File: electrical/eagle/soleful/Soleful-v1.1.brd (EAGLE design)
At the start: 50.5 x 59.7 mm, 118 parts, among them CN1 To Battery, CN2 Ext Power, IC1 STM32F405RGT, IC2 LT1129-3.3, IC3 MCP73833-UN, Q4 32.768kHz, SW1 RST, U1 USB Power, U2 TPD3E001DRLR, Y1 12 MHz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

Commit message: finished board layout bitch
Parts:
- moved U2 129.9 mm to (10.8, 5.71)
- moved R30 124.3 mm to (35.2, 17.4), turned to 180 degrees
- moved R14 123.1 mm to (45.1, 22.9), turned to 180 degrees
- moved R23 120.3 mm to (35.2, 18.6), turned to 180 degrees
- moved R12 113.7 mm to (44.5, 27.9)
- moved R11 110.8 mm to (44.5, 25.4)
- moved R15 104.1 mm to (18.7, 16.8), turned to 90 degrees
- moved TP6 97.0 mm to (41.2, 19.5)
- moved R10 96.1 mm to (17.3, 3.27), turned to 180 degrees
- moved TP4 93.9 mm to (48.9, 28.6)
- moved C10 93.6 mm to (36.1, 7.94), turned to 270 degrees
- moved R13 91.8 mm to (17.4, 27.3), turned to 180 degrees
- moved R3 91.8 mm to (37.5, 30.5)
- moved D6 90.9 mm to (10.2, 16.5), turned to 270 degrees
- moved TP3 90.7 mm to (48.9, 30.5)
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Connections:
- removed net N$19: U$18.10
- removed net N$23: R41.2
- net N$16: now also R41.2, U$18.10; no longer U$18.11
- net VDD-MMA: now also U$18.11
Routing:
- net 3V3: track 0.00 -> 267.1 mm, vias 0 -> 10
- net RST-WIFI: track 0.00 -> 145.7 mm, vias 0 -> 6
- net EN-WIFI: track 0.00 -> 144.1 mm, vias 0 -> 2
- net RX-WIFI: track 0.00 -> 97.2 mm, vias 0 -> 4
- net TX-WIFI: track 0.00 -> 94.9 mm, vias 0 -> 4
- net VDD-MMA: track 0.00 -> 62.6 mm, vias 0 -> 2
- net VUSB: track 0.00 -> 57.9 mm, vias 0 -> 4
- net RST-IMU: track 0.00 -> 57.3 mm, vias 0 -> 2
- net V+: track 0.00 -> 52.7 mm, vias 0 -> 2
- net PWR-IMU: track 0.00 -> 50.2 mm, vias 0 -> 6
- net PB2-BOOT1-MMA-INT: track 0.00 -> 48.0 mm, vias 0 -> 4
- net SCL-IMU: track 0.00 -> 43.5 mm, vias 0 -> 3
- net VCC-WIFI: track 0.00 -> 43.5 mm, vias 0 -> 2
- net PC11-SDIO_D3: track 0.00 -> 43.2 mm, vias 0 -> 2
- net SDA-IMU: track 0.00 -> 42.9 mm, vias 0 -> 2
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
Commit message: fixed all DRC issues
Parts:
- moved R30 0.27 mm to (35.2, 17.1)
- moved X1 0.13 mm to (9.02, 46.4)
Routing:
- net VCC-WIFI: track 43.5 -> 48.1 mm
- net 3V3: track 267.1 -> 265.2 mm, vias 10 -> 9
- net PWR-WIFI: track 42.3 -> 43.4 mm
- net PB2-BOOT1-MMA-INT: track 48.0 -> 48.7 mm
- net RST-WIFI: track 145.7 -> 146.3 mm

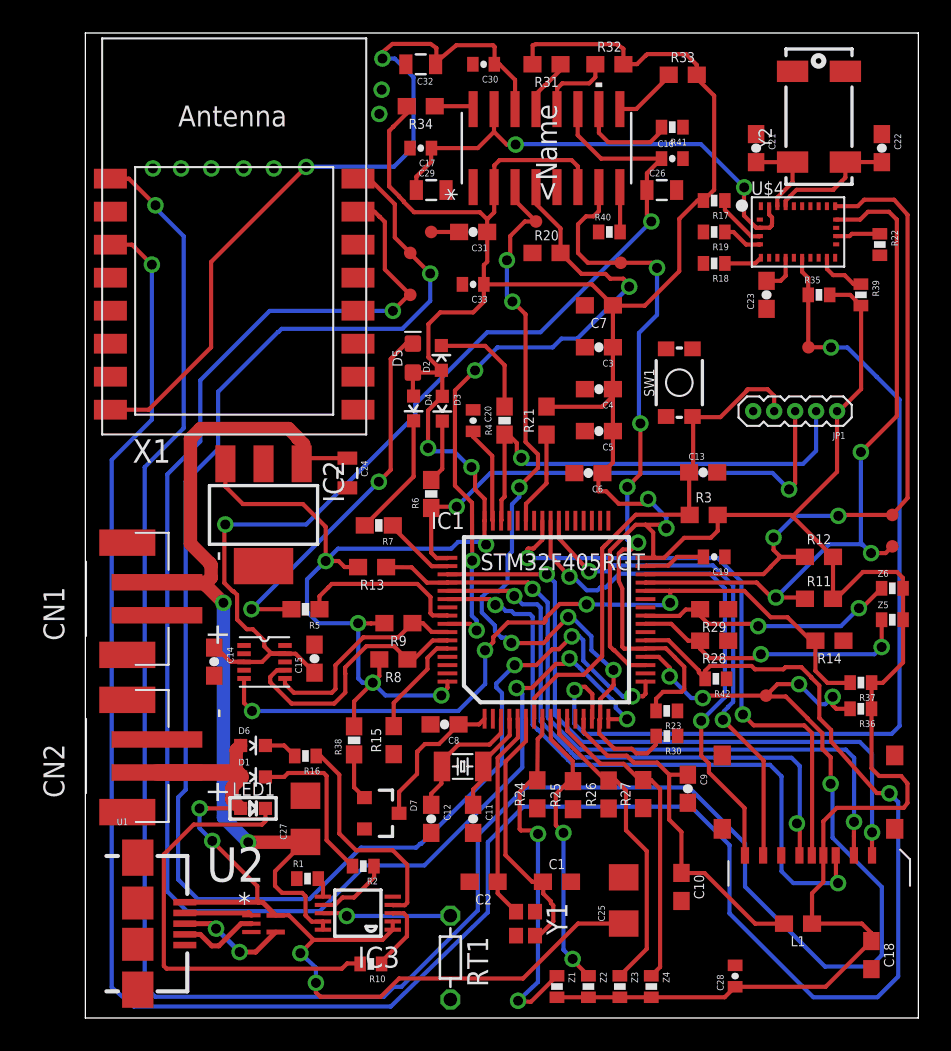
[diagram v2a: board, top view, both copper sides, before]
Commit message: finished the entire layout based on Sunstones DRC rules bitches
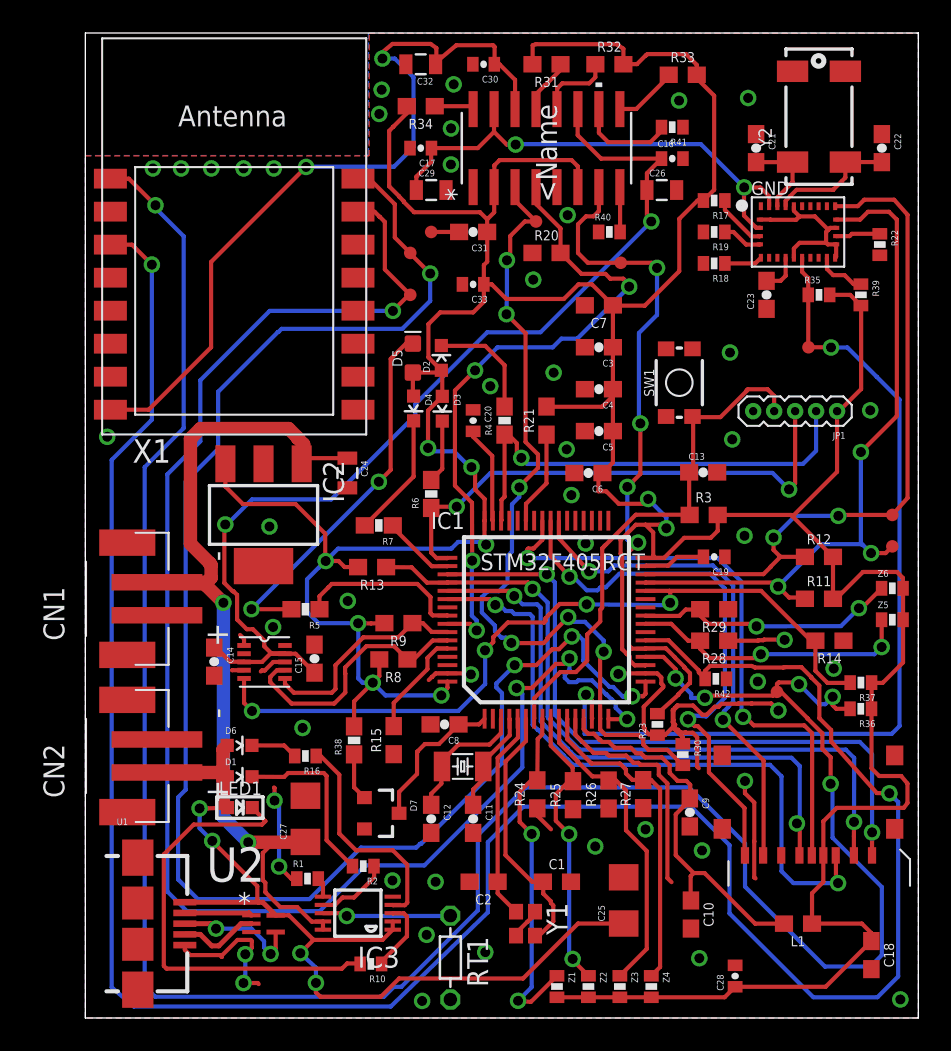
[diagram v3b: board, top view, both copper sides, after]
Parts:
- moved C10 1.77 mm to (36.7, 6.27)
- moved R30 1.48 mm to (36.2, 16.0), turned to 270 degrees
- moved C9 1.44 mm to (36.6, 12.5)
- moved R23 1.00 mm to (34.7, 17.8), turned to 90 degrees
- moved D6 0.81 mm to (9.35, 16.5)
- moved D1 0.81 mm to (9.35, 14.6)
- moved LED1 0.80 mm to (9.36, 12.7)
- moved TP6 0.70 mm to (41.9, 19.8)
- renumbered U$4 to GND
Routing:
- net GND: track 1.69 -> 84.2 mm, vias 0 -> 42
- net RST-IMU: track 57.5 -> 55.5 mm
- net VUSB: track 57.7 -> 55.9 mm
- net V+: track 52.7 -> 54.3 mm
- net A3V3: track 21.9 -> 23.4 mm
- net PC9-SDIO_D1: track 32.2 -> 33.6 mm
- net TX-WIFI: track 94.4 -> 95.6 mm
- net PWR-WIFI: track 43.4 -> 42.2 mm
- net N$27: track 6.72 -> 7.64 mm
- net PWR-IMU: track 50.3 -> 51.2 mm
- net ADC-FSR1: track 22.3 -> 21.5 mm
- net N$14: track 2.04 -> 2.85 mm
- net N$10: track 10.00 -> 10.8 mm
- net ADC-FSR4: track 19.3 -> 20.0 mm
- added copper zone on layer 1, net GND
- added copper zone on layer 16, net GND
